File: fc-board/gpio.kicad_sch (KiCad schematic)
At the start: 25 parts, among them J14 sdcard, T1 SM91509AL-E, U1 74LVC1G07SE-7

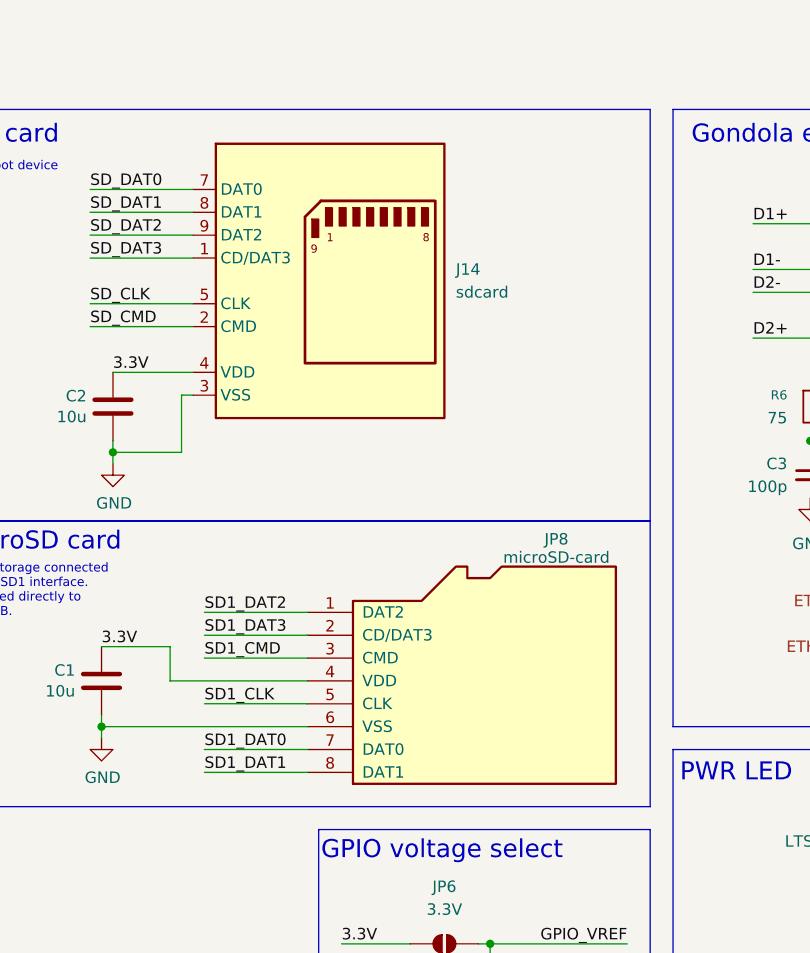
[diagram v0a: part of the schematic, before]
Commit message: Properly placed the Harwin connectors according to key
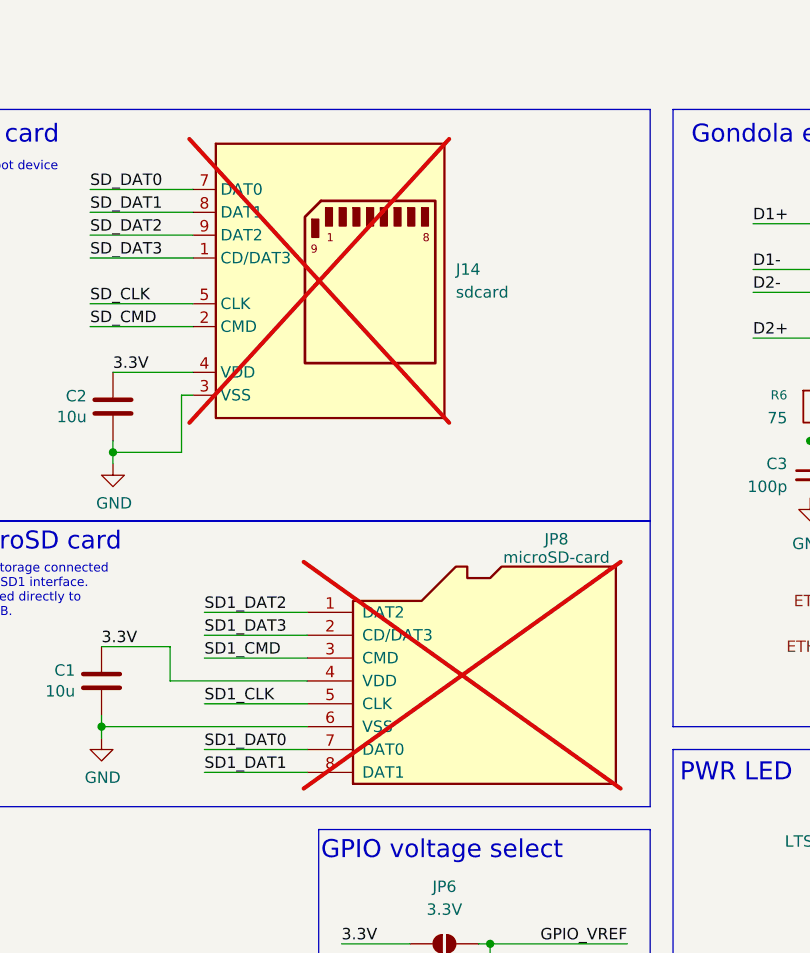
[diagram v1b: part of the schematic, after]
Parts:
- J14, JP8: now not fitted; now left out of the parts list
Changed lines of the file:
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@@
 		(unit 1)
 		(exclude_from_sim no)
-		(in_bom yes)
+		(in_bom no)
 		(on_board yes)
-		(dnp no)
+		(dnp yes)
 		(fields_autoplaced yes)
 		(property "Reference" "J14"
@@
 		(unit 1)
 		(exclude_from_sim no)
-		(in_bom yes)
+		(in_bom no)
 		(on_board yes)
-		(dnp no)
+		(dnp yes)
 		(property "Reference" "JP8"
 			(at 201.676 62.992 0)

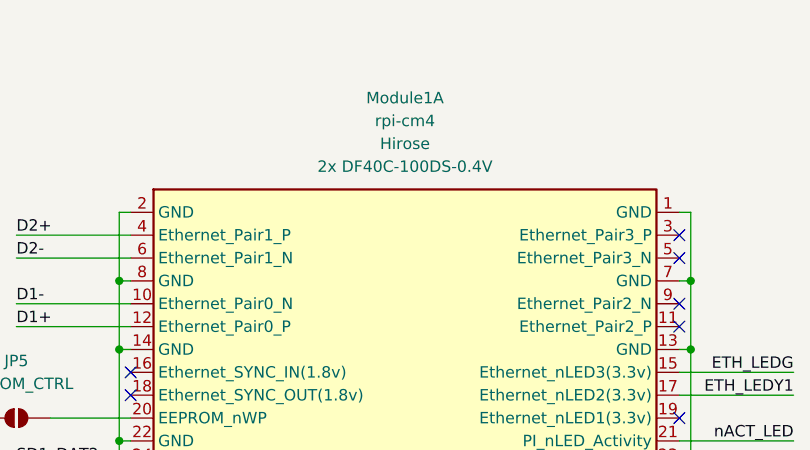
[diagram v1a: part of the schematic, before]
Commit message: Fleshed out part numbers and design rules
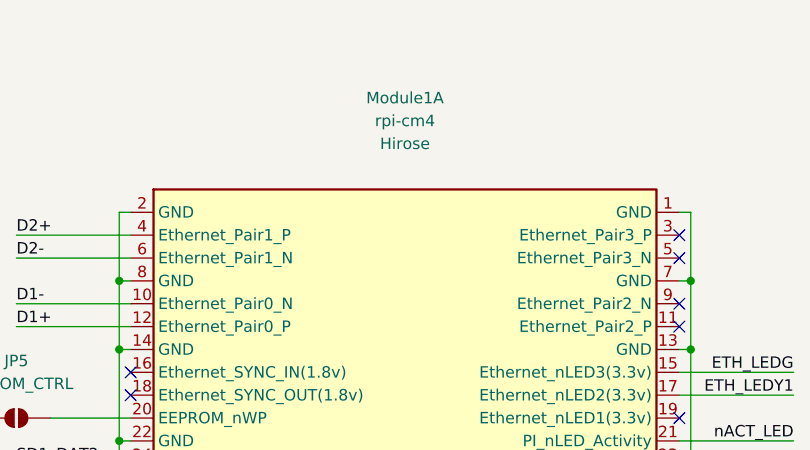
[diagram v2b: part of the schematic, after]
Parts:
- Module1: Field5 2x DF40C-100DS-0.4V -> (none)

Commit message: AdvancedPCB specs met
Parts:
- C3: now not fitted
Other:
- note added: "Marked as DNP for AdvancedPCB"
